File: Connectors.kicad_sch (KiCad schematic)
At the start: 19 parts

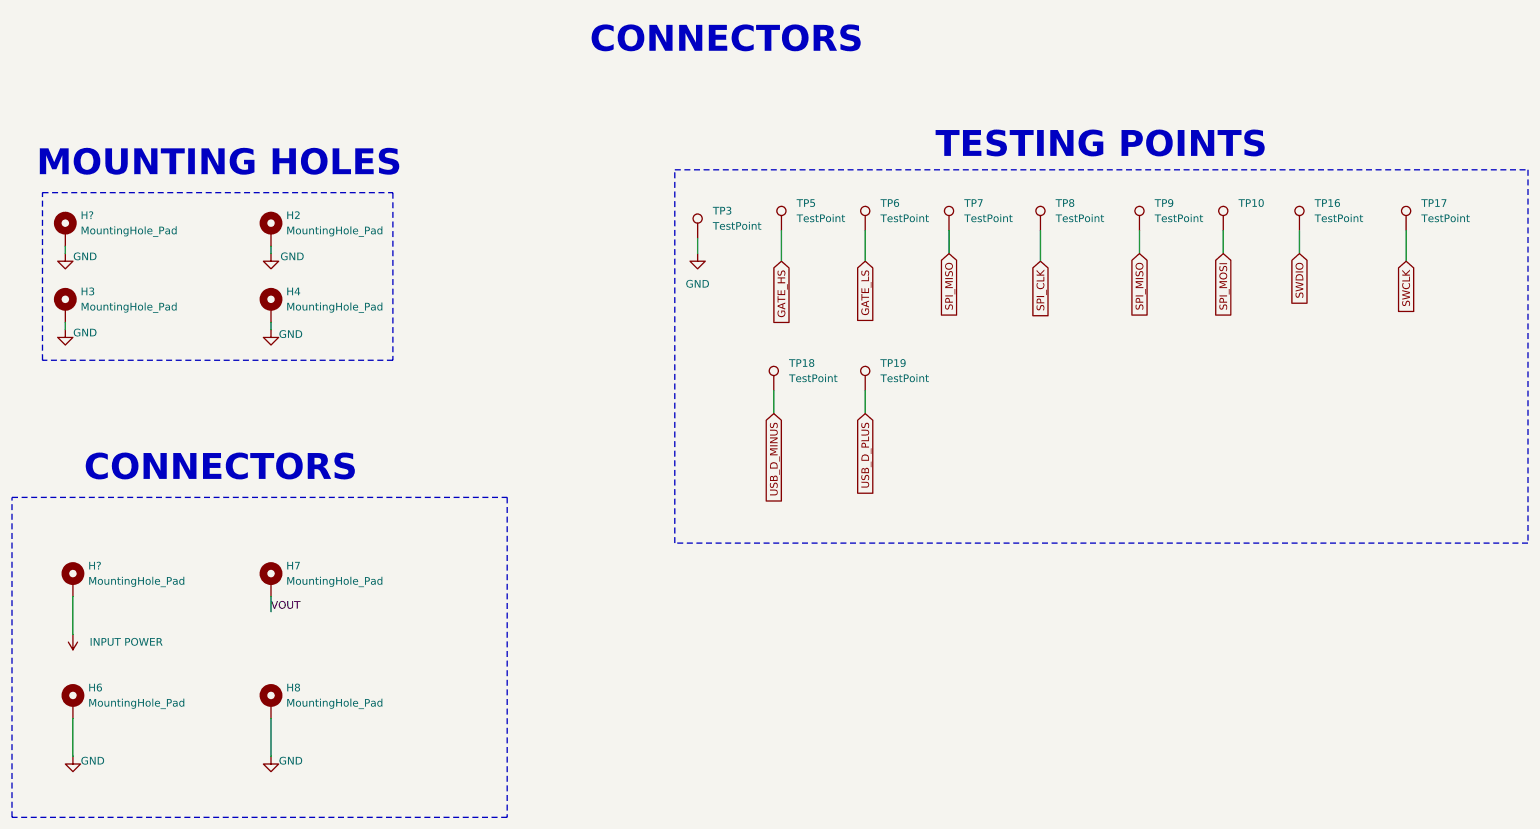
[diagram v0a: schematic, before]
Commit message: Placement finished routing started
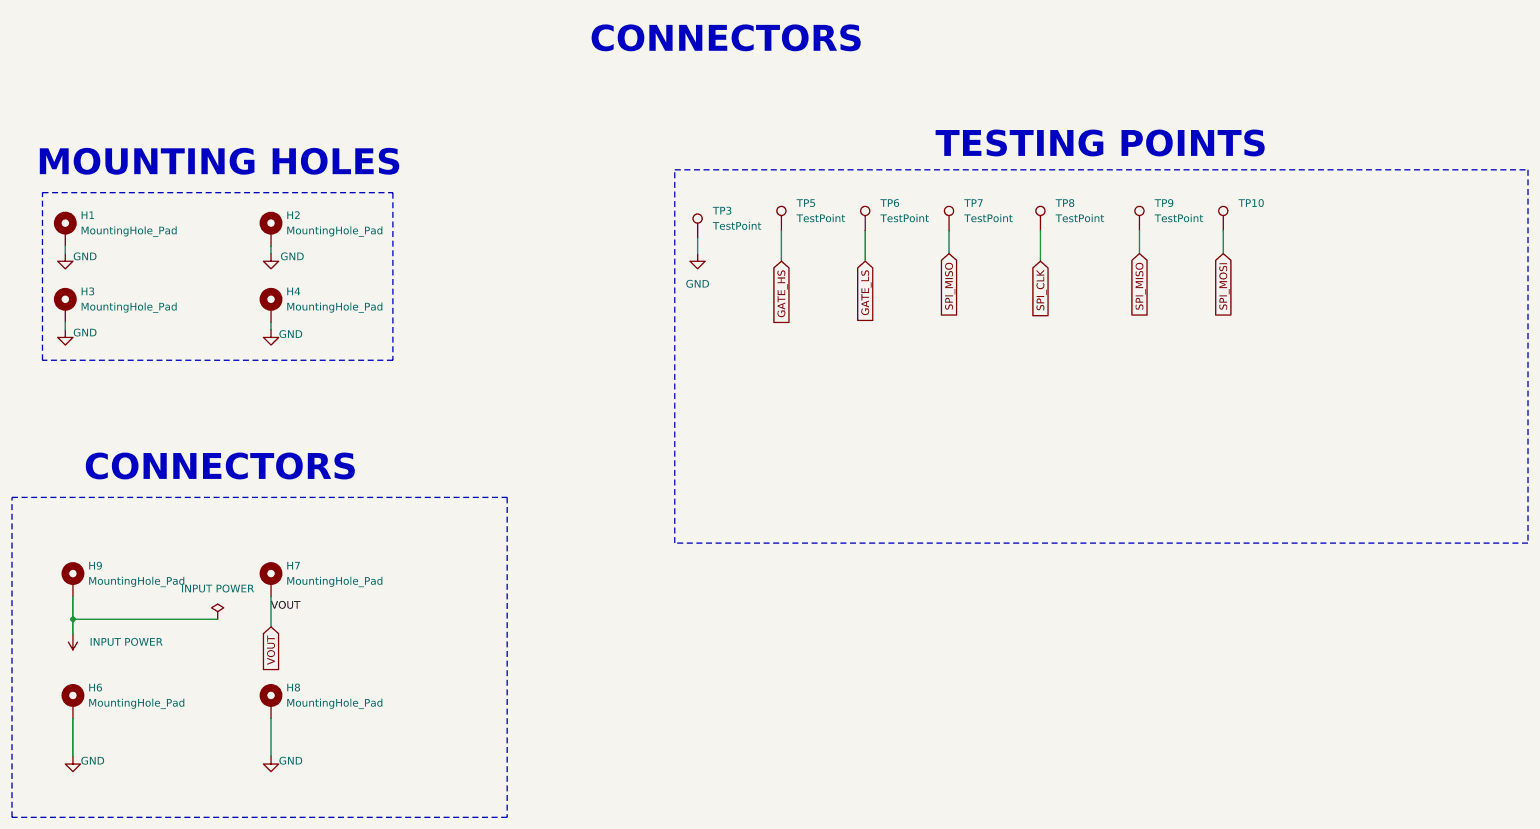
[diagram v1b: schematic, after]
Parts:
- removed TP16, TP17, TP18, TP19: TestPoint, TestPoint:TestPoint_Loop_D2.54mm_Drill1.5mm_Beaded, symbol Connector:TestPoint
- gave numbers to parts that had none: 2
